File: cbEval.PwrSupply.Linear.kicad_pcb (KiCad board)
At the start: 2 copper layers, 35 x 109 mm, 34 parts, among them J1 CAL.CT3151V1-0, J11 Bergstik-II_6, J12 Header.Hor.2x8.9-103326-0-08, J13 Header.Hor.2x8.9-103326-0-08, J2 CAL.CT3151V1-2, J3 Socket.Hor.2x8.1-5535512-8, J4 Socket.Hor.2x8.1-5535512-8, U1 MIC29151-5.0WU, U2 MIC29151-3.3WU, U3 DS1834AS+

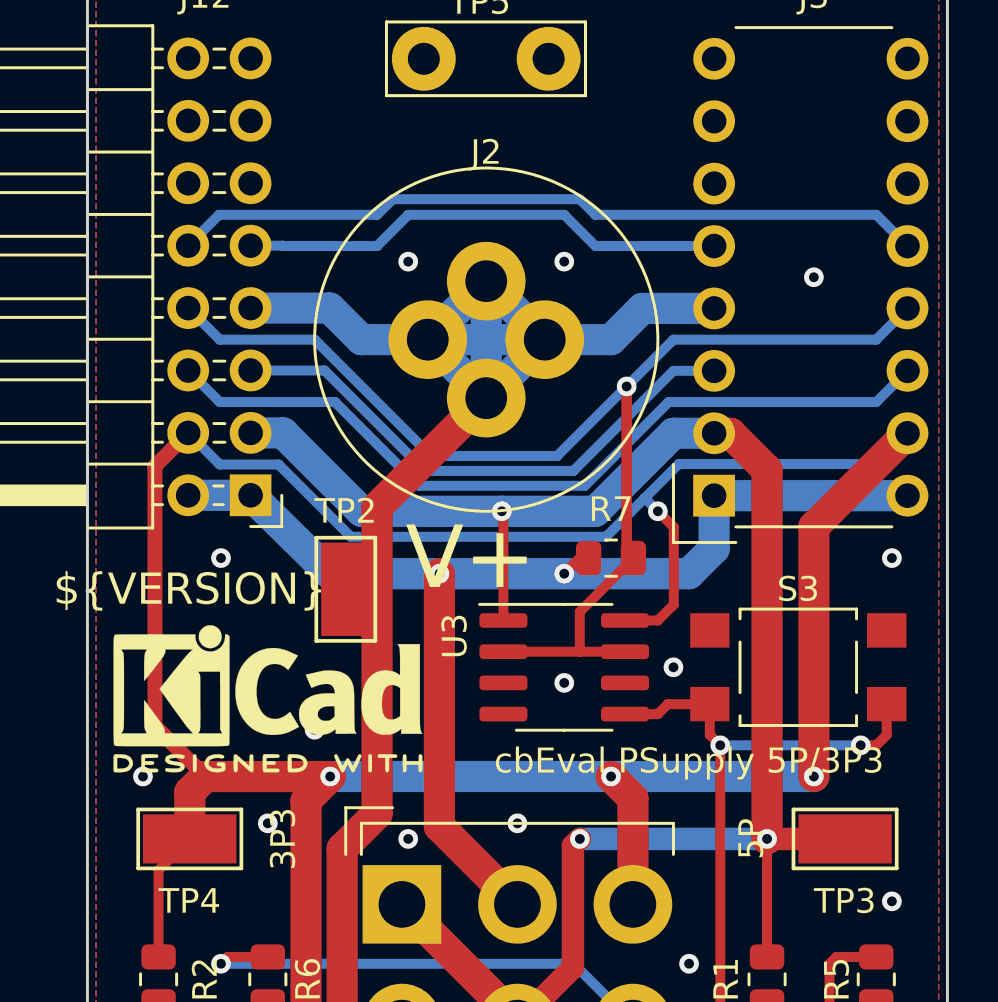
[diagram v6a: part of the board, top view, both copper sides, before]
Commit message: Stromversorgung korrigiert (5P/3P3)
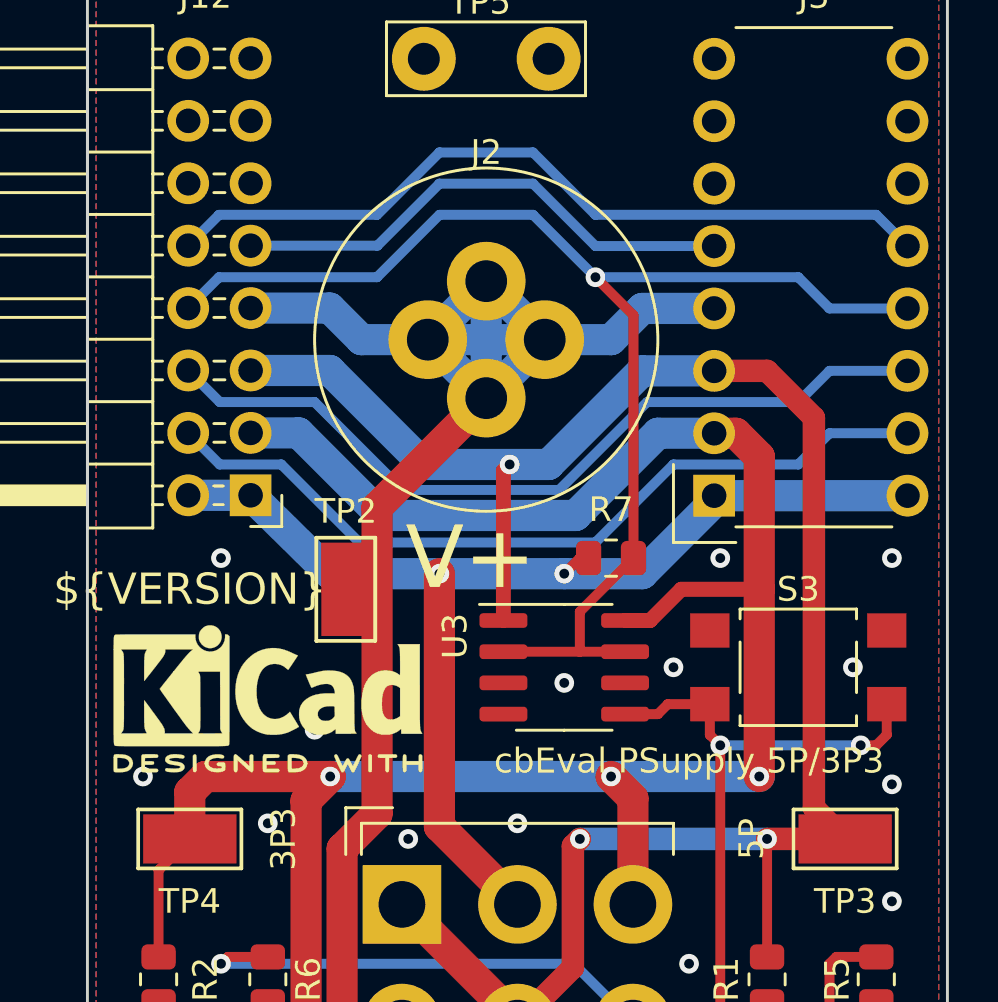
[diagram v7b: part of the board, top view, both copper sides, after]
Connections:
- J12 pad 3: +5V -> +3V3
- J12 pad 4: +3V3 -> +15V
- J12 pad 5: +15V -> +5V
- J3 pad 3: +5V -> +3V3
- J3 pad 4: +3V3 -> +15V
- J3 pad 5: +15V -> +5V
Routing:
- net +3V3: track 141.2 -> 111.1 mm, vias 4 -> 3
- net +15V: track 22.2 -> 33.0 mm
- net +5V: track 98.3 -> 105.6 mm
- net ~RESET: track 57.4 -> 54.2 mm
- net /I2C-SCL: track 30.8 -> 32.4 mm
- net VCC: track 49.2 -> 48.1 mm
- net /I2C-SDA: track 19.9 -> 21.0 mm

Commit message: gespeichert im neuen Format
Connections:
- net /SPI-~CE renamed /SPI-~{CE}
- net ~PWR-FAIL renamed ~{PWR-FAIL}
- net ~RESET renamed ~{RESET}
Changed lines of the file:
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@@
-(kicad_pcb (version 20210424) (generator pcbnew)
+(kicad_pcb (version 20210623) (generator pcbnew)
   (general
     (thickness 1.6)
@@
   (net 3 "+5V")
   (net 4 "+3V3")
-  (net 5 "~RESET")
+  (net 5 "~{RESET}")
   (net 6 "Net-(D1-Pad4)")
   (net 7 "Net-(D2-Pad4)")
@@
   (net 18 "Net-(R5-Pad1)")
   (net 19 "Net-(R6-Pad1)")
-  (net 20 "~PWR-FAIL")
+  (net 20 "~{PWR-FAIL}")
   (net 21 "-15V")
   (net 22 "+15V")
@@
   (net 25 "/SPI-ADR1")
   (net 26 "/SPI-ADR0")
-  (net 27 "/SPI-~CE")
+  (net 27 "/SPI-~{CE}")
   (net 28 "/SPI-CLK")
   (net 29 "/SPI-MRST")
@@
       (net 28 "/SPI-CLK") (pinfunction "11") (pintype "passive"))
     (pad "12" thru_hole circle (at 0 -5.08) (size 1.7 1.7) (drill 1) (layers *.Cu *.Mask)
-      (net 27 "/SPI-~CE") (pinfunction "12") (pintype "passive"))
+      (net 27 "/SPI-~{CE}") (pinfunction "12") (pintype "passive"))
     (pad "13" thru_hole circle (at -7.869999 -7.62) (size 1.7 1.7) (drill 1) (layers *.Cu *.Mask)
       (net 26 "/SPI-ADR0") (pinfunction "13") (pintype "passive"))
@@
       (net 12 "+VDC") (pinfunction "7") (pintype "passive"))
     (pad "8" thru_hole circle (at 0 0) (size 1.7 1.7) (drill 1) (layers *.Cu *.Mask)
-      (net 5 "~RESET") (pinfunction "8") (pintype "passive"))
+      (net 5 "~{RESET}") (pinfunction "8") (pintype "passive"))
     (pad "9" thru_hole circle (at -7.87 -2.54) (size 1.7 1.7) (drill 1) (layers *.Cu *.Mask)
       (net 24 "/I2C-SDA") (pinfunction "9") (pintype "passive"))
@@
       (net 3 "+5V") (pinfunction "OUT") (pintype "power_out"))
     (pad "5" smd rect locked (at -5.775 3.4 270) (size 4.6 1.1) (layers "F.Cu" "F.Paste" "F.Mask")
-      (net 20 "~PWR-FAIL") (pinfunction "FLG") (pintype "open_collector"))
+      (net 20 "~{PWR-FAIL}") (pinfunction "FLG") (pintype "open_collector"))
     (model "${KICAD6_3DMODEL_DIR}/Package_TO_SOT_SMD.3dshapes/TO-263-5_TabPin3.wrl"
       (offset (xyz 0 0 0))
@@
       (net 3 "+5V") (pinfunction "5V-IN") (pintype "power_in"))
     (pad "2" smd roundrect locked (at -2.475 -0.635) (size 1.95 0.6) (layers "F.Cu" "F.Paste" "F.Mask") (roundrect_rratio 0.25)
-      (net 5 "~RESET") (pinfunction "5V-~RST") (pintype "open_collector"))
+      (net 5 "~{RESET}") (pinfunction "5V-~RST") (pintype "open_collector"))
     (pad "3" smd roundrect locked (at -2.475 0.635) (size 1.95 0.6) (layers "F.Cu" "F.Paste" "F.Mask") (roundrect_rratio 0.25)
       (net 2 "GND") (pinfunction "5V-TOL") (pintype "passive"))
@@
       (net 2 "GND") (pinfunction "GND") (pintype "power_in"))
     (pad "5" smd roundrect locked (at 2.475 1.905) (size 1.95 0.6) (layers "F.Cu" "F.Paste" "F.Mask") (roundrect_rratio 0.25)
-      (net 20 "~PWR-FAIL") (pinfunction "~PBRST") (pintype "passive"))
+      (net 20 "~{PWR-FAIL}") (pinfunction "~PBRST") (pintype "passive"))
     (pad "6" smd roundrect locked (at 2.475 0.635) (size 1.95 0.6) (layers "F.Cu" "F.Paste" "F.Mask") (roundrect_rratio 0.25)
       (net 2 "GND") (pinfunction "3.3V-TOL") (pintype "passive"))
     (pad "7" smd roundrect locked (at 2.475 -0.635) (size 1.95 0.6) (layers "F.Cu" "F.Paste" "F.Mask") (roundrect_rratio 0.25)
-      (net 5 "~RESET") (pinfunction "3.3V-~RST") (pintype "open_collector"))
+      (net 5 "~{RESET}") (pinfunction "3.3V-~RST") (pintype "open_collector"))
     (pad "8" smd roundrect locked (at 2.475 -1.905) (size 1.95 0.6) (layers "F.Cu" "F.Paste" "F.Mask") (roundrect_rratio 0.25)
       (net 4 "+3V3") (pinfunction "3.3V-IN") (pintype "power_in"))
@@
       (net 12 "+VDC") (pinfunction "7") (pintype "passive"))
     (pad "8" thru_hole oval locked (at 2.54 7.62 180) (size 1.7 1.7) (drill 1) (layers *.Cu *.Mask)
-      (net 5 "~RESET") (pinfunction "8") (pintype "passive"))
+      (net 5 "~{RESET}") (pinfunction "8") (pintype "passive"))
     (pad "9" thru_hole oval locked (at 0 10.16 180) (size 1.7 1.7) (drill 1) (layers *.Cu *.Mask)
       (net 24 "/I2C-SDA") (pinfunction "9") (pintype "passive"))
@@
     (fp_circle (center 0 0) (end 1.25 0) (layer "F.Fab") (width 0.1) (fill none))
     (pad "1" smd rect locked (at -3.6 -1.5 180) (size 1.6 1.4) (layers "F.Cu" "F.Paste" "F.Mask")
-      (net 20 "~PWR-FAIL") (pinfunction "1") (pintype "passive"))
+      (net 20 "~{PWR-FAIL}") (pinfunction "1") (pintype "passive"))
     (pad "1" smd rect locked (at 3.6 -1.5 180) (size 1.6 1.4) (layers "F.Cu" "F.Paste" "F.Mask")
-      (net 20 "~PWR-FAIL") (pinfunction "1") (pintype "passive"))
+      (net 20 "~{PWR-FAIL}") (pinfunction "1") (pintype "passive"))
     (pad "2" smd rect locked (at 3.6 1.5 180) (size 1.6 1.4) (layers "F.Cu" "F.Paste" "F.Mask")
       (net 2 "GND") (pinfunction "2") (pintype "passive"))
@@
       (net 4 "+3V3") (pinfunction "OUT") (pintype "power_out"))
     (pad "5" smd rect locked (at -5.775 3.4 270) (size 4.6 1.1) (layers "F.Cu" "F.Paste" "F.Mask")
-      (net 20 "~PWR-FAIL") (pinfunction "FLG") (pintype "open_collector"))
+      (net 20 "~{PWR-FAIL}") (pinfunction "FLG") (pintype "open_collector"))
     (model "${KICAD6_3DMODEL_DIR}/Package_TO_SOT_SMD.3dshapes/TO-263-5_TabPin3.wrl"
       (offset (xyz 0 0 0))
@@
       (net 28 "/SPI-CLK") (pinfunction "11") (pintype "passive"))
     (pad "12" thru_hole oval locked (at 2.54 12.7 180) (size 1.7 1.7) (drill 1) (layers *.Cu *.Mask)
-      (net 27 "/SPI-~CE") (pinfunction "12") (pintype "passive"))
+      (net 27 "/SPI-~{CE}") (pinfunction "12") (pintype "passive"))
     (pad "13" thru_hole oval locked (at 0 15.24 180) (size 1.7 1.7) (drill 1) (layers *.Cu *.Mask)
       (net 26 "/SPI-ADR0") (pinfunction "13") (pintype "passive"))
@@
       (net 1 "VCC") (pintype "passive"))
     (pad "2" smd roundrect locked (at 0.9125 0) (size 1.025 1.4) (layers "F.Cu" "F.Paste" "F.Mask") (roundrect_rratio 0.243902)
-      (net 5 "~RESET") (pintype "passive"))
+      (net 5 "~{RESET}") (pintype "passive"))
     (model "${KICAD6_3DMODEL_DIR}/Resistor_SMD.3dshapes/R_0805_2012Metric.wrl"
       (offset (xyz 0 0 0))
